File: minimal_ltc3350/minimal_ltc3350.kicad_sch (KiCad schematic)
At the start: 43 parts, among them Q1 20.0 V, Q2 20.0 V, Q3 20 V, Q4 20 V, U1 LTC3350EUHF-PBF

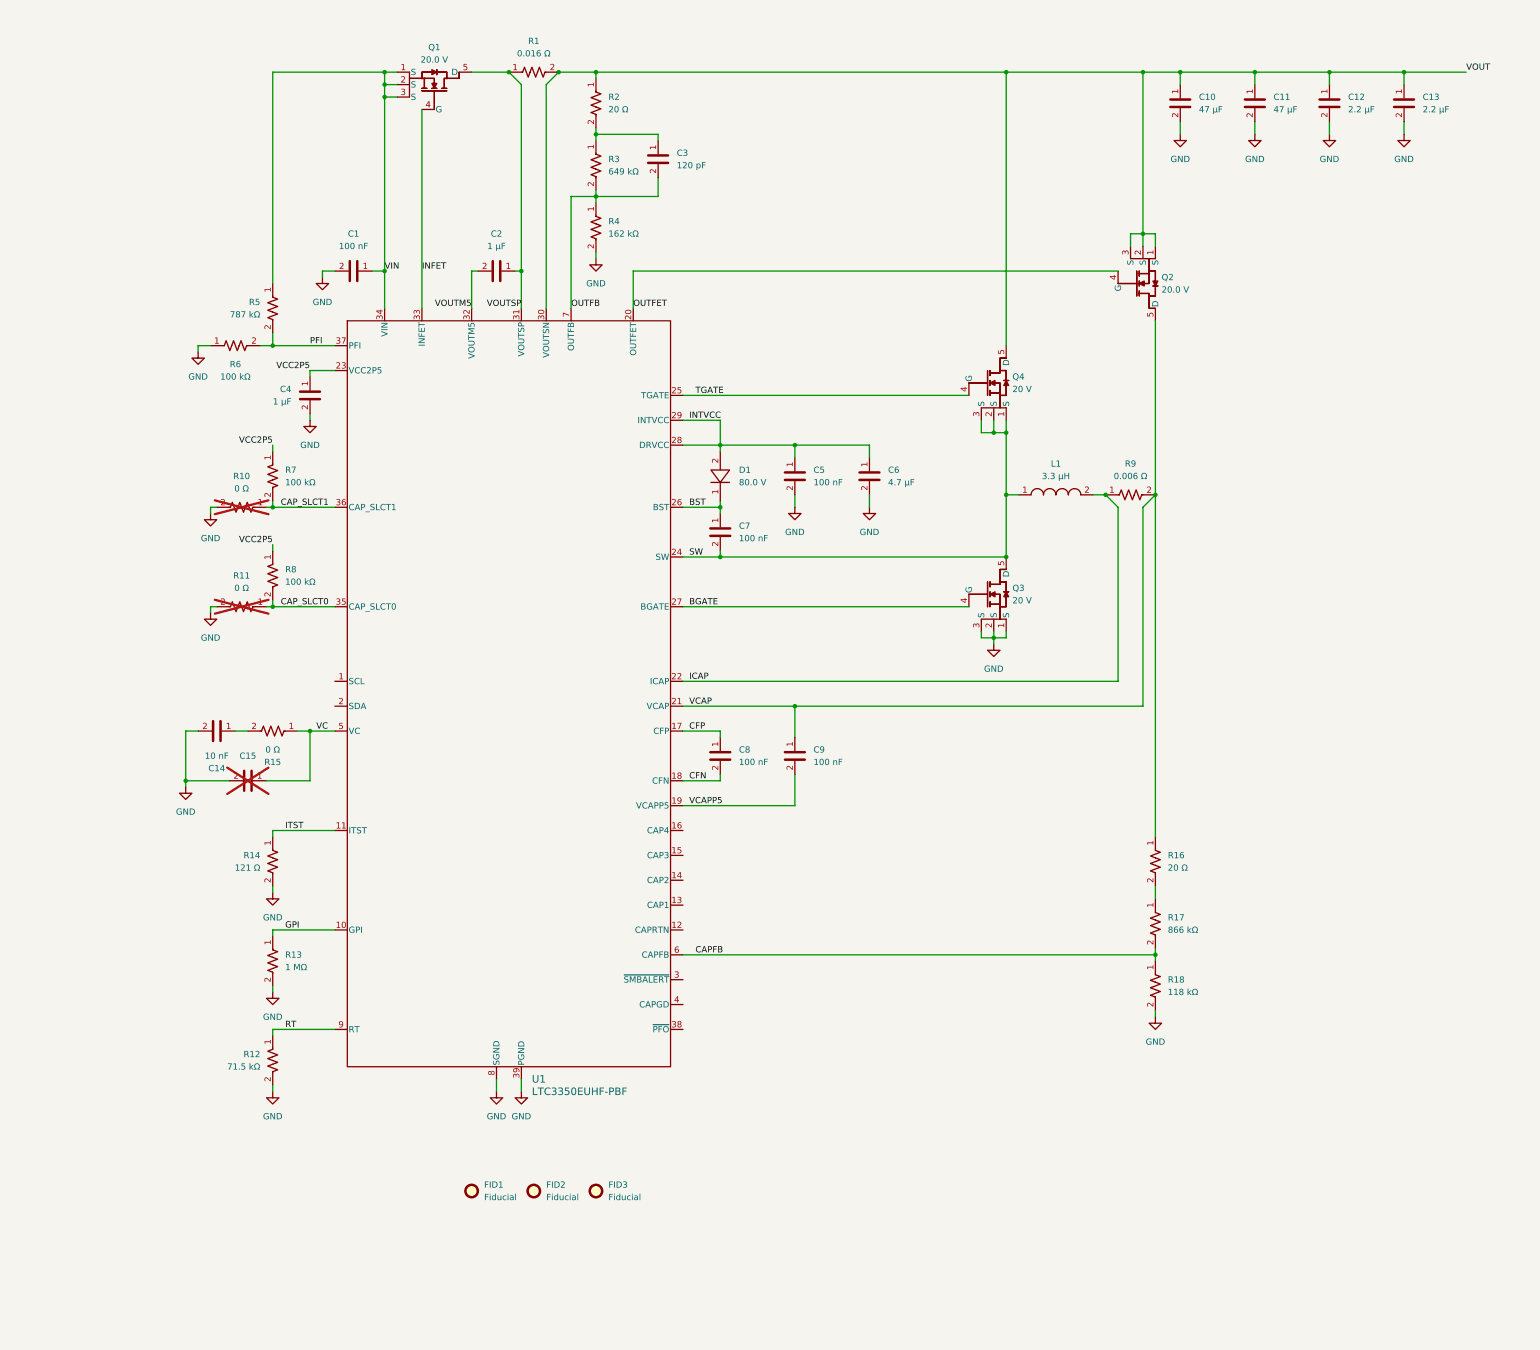
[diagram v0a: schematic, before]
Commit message: Add C19 capacitor and update component positions in KiCad project
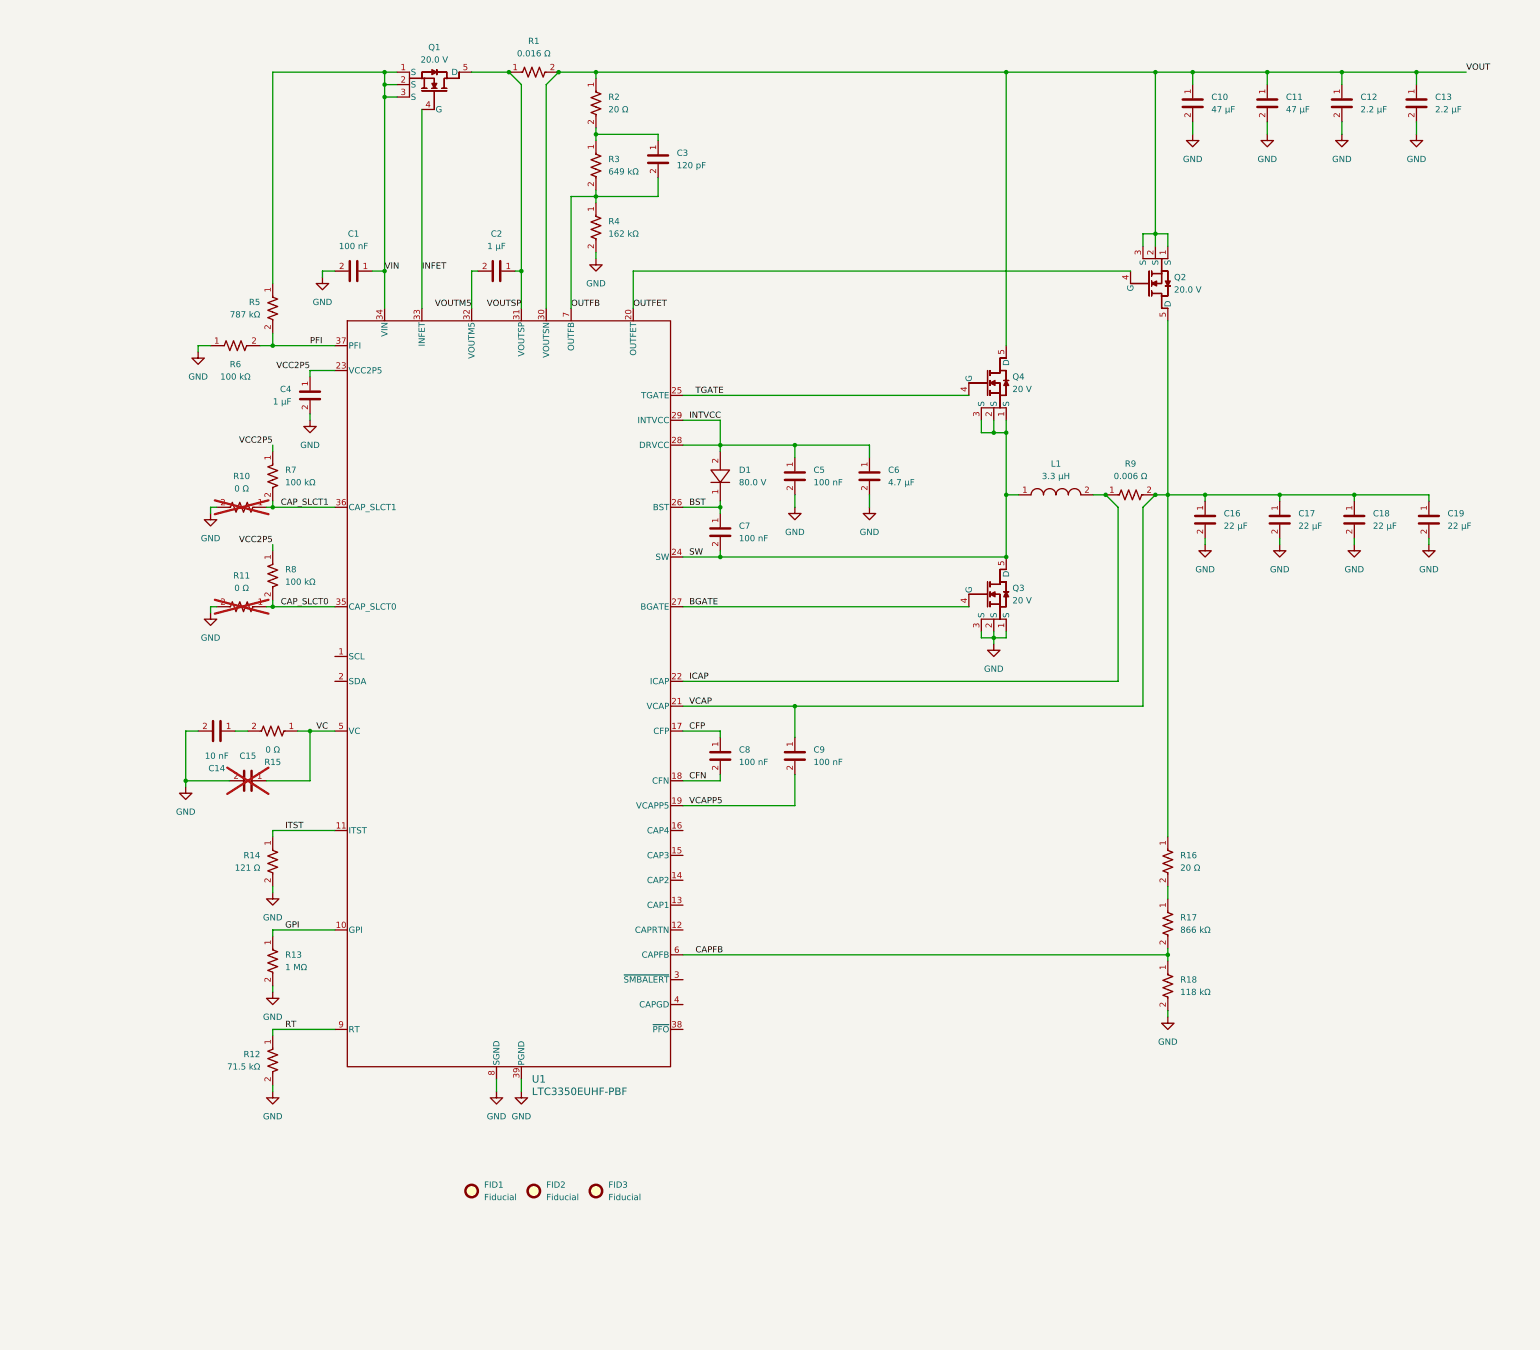
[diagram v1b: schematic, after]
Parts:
- added C16, C17, C18, C19: 22 µF, capacitor_footprints:C_0805_2012Metric, symbol CAPACITORS_C2012X5R1C_DATA_BASE:C_C2012X5R1C226M125AC
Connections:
- net GND: now also C16.2, C17.2, C18.2, C19.2
- net VCAP: now also C16.1, C17.1, C18.1, C19.1
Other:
- moved on the sheet: C10, C11, C12, C13, Q2, R16, R17, R18

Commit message: Update KiCAD project files and symbols generator
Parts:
- added R19, R20, R21, R22, R23: 2.7 Ω, resistor_footprints:R_0805_2012Metric, symbol RESISTORS_ERJ-6DQF_DATA_BASE:R_ERJ-6DQF2R7V
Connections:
- net GND: now also R23.2
- net VCAP: now also R19.2
- net CAPRTN: now reaches U1.12 (CAPRTN)
- net CAPRTN: now also R23.1
- net CAP1: now reaches U1.13 (CAP1)
- net CAP1: now also R22.1
- net CAP2: now reaches U1.14 (CAP2)
- net CAP2: now also R21.1
- net CAP3: now reaches U1.15 (CAP3)
- net CAP3: now also R20.1
- net CAP4: now reaches U1.16 (CAP4)
- net CAP4: now also R19.1
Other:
- moved on the sheet: C1, C10, C11, C12, C13, C14, C15, C16, C17, C18, C19, C2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

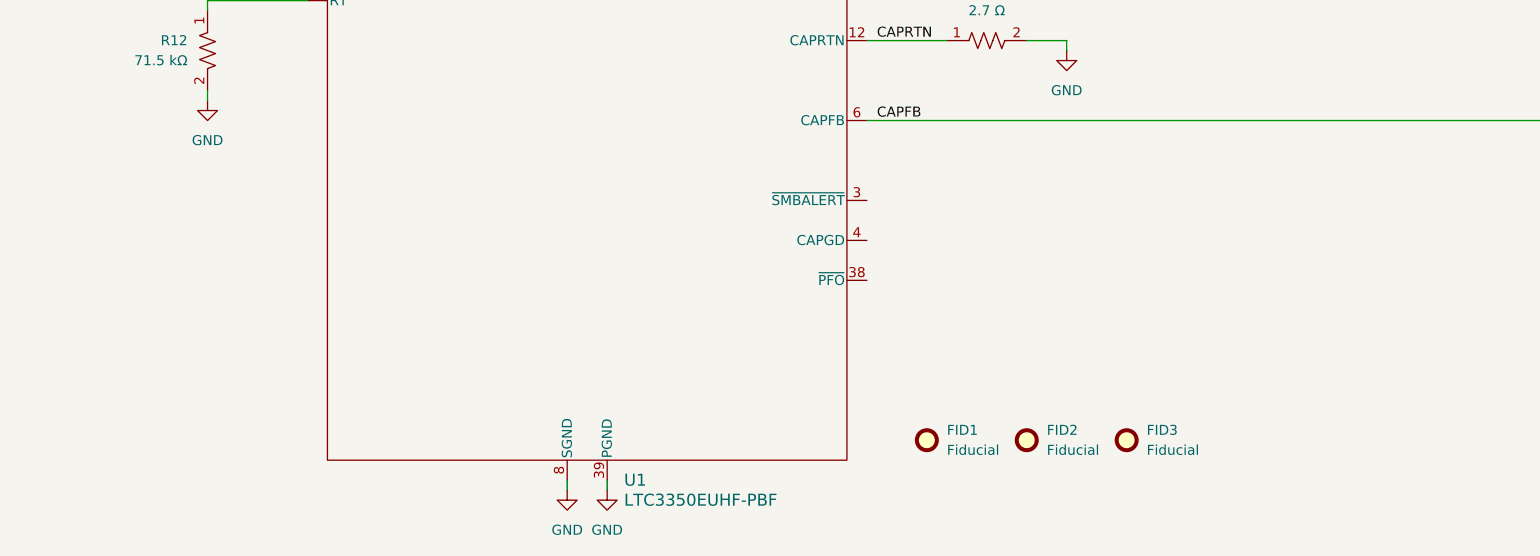
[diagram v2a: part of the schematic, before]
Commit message: Update KiCad project: Add LED components and adjust resistor positions
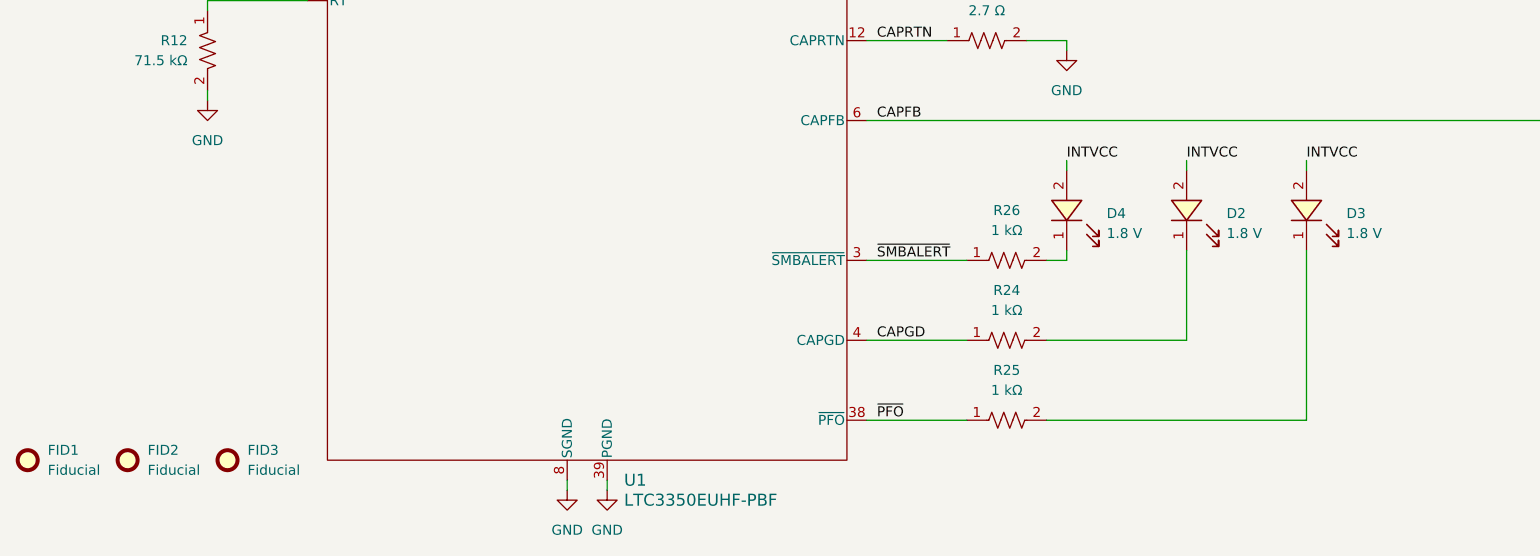
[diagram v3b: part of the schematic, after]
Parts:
- added D2, D3, D4: 1.8 V, diode_footprints:LED_RED_0402_1005Metric, symbol DIODES_APHHS1005LSECK-J3-PF_DATA_BASE:D_APHHS1005LSECK-J3-PF
- added R24, R25, R26: 1 kΩ, resistor_footprints:R_0402_1005Metric, symbol RESISTORS_ERJ-2RKF_DATA_BASE:R_ERJ-2RKF1001X
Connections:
- net INTVCC: now also D2.2, D3.2, D4.2
- net ~{SMBALERT}: now reaches U1.3 (~{SMBALERT})
- net ~{SMBALERT}: now also R26.1
- net ~{PFO}: now reaches U1.38 (~{PFO})
- net ~{PFO}: now also R25.1
- net CAPGD: now reaches U1.4 (CAPGD)
- net CAPGD: now also R24.1
- new net: D2.1, R24.2
- new net: D4.1, R26.2
- new net: D3.1, R25.2
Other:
- moved on the sheet: FID1, FID2, FID3

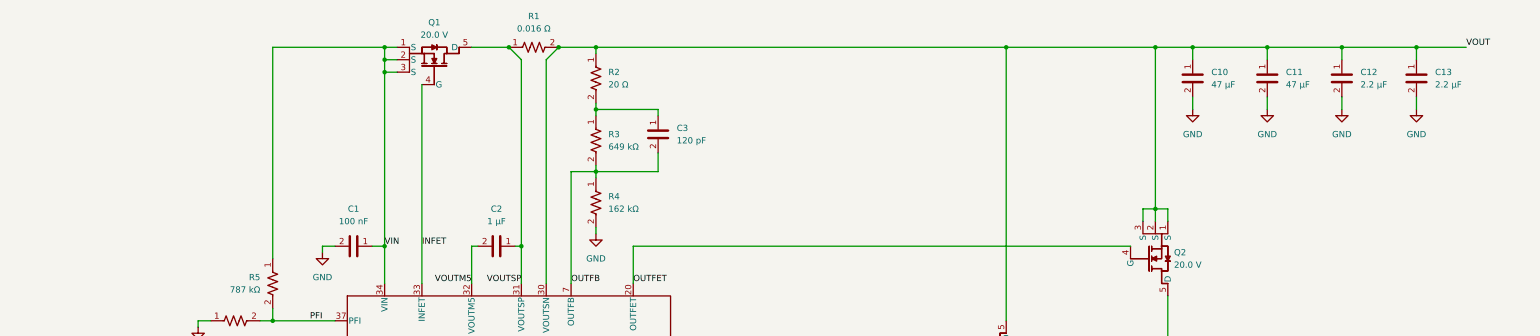
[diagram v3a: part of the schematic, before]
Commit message: Update KiCad project: Update PCB layout and schematic
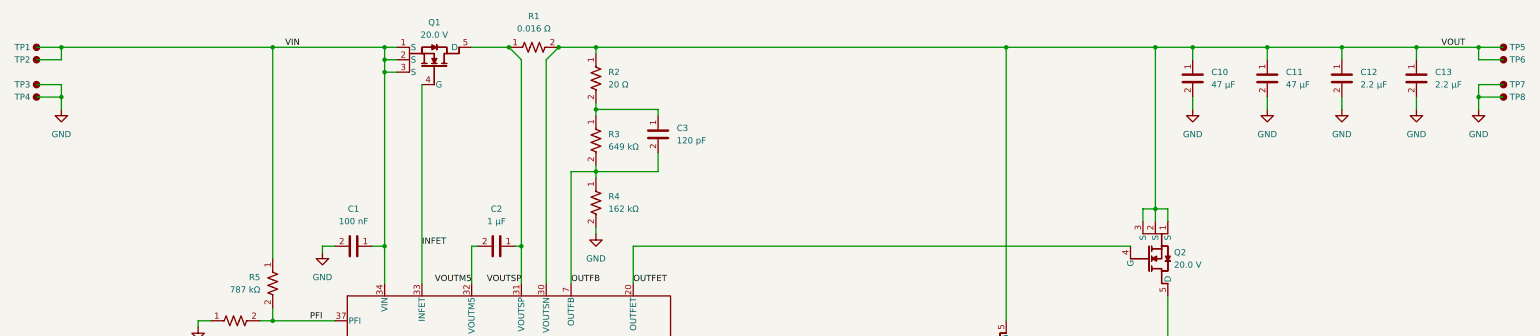
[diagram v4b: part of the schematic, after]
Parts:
- added TP1, TP2, TP3, TP4, TP5, TP6, TP7, TP8: TestPoint, test_point_footprints:TestPoint_THTPad_Castelated, symbol UNITED_TEST_POINTS:TestPoint_Castelated_v2
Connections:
- net GND: now also TP3.1, TP4.1, TP7.1, TP8.1
- net VIN: now also TP1.1, TP2.1
- net VOUT: now also TP5.1, TP6.1

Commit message: Update KiCAD files and symbol table
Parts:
- removed R14: 121 Ω, resistor_footprints:R_0402_1005Metric, symbol RESISTORS_ERJ-2RKF_DATA_BASE:R_ERJ-2RKF1210X
- added Q5: 20.0 V, transistor_footprints:SOT23, symbol TRANSISTORS_SI2374DS-T1-BE3_DATA_BASE:Q_SI2374DS-T1-BE3
- added R27: 10 MΩ, resistor_footprints:R_0402_1005Metric, symbol RESISTORS_RC0402FR-07_DATA_BASE:R_RC0402FR-0710ML
- added R28, R29: 100 Ω, resistor_footprints:R_2512_6332Metric, symbol RESISTORS_SR2512FK-7W_DATA_BASE:R_SR2512FK-7W100RL
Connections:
- net GND: now also Q5.3 (D), R27.2
- net ITST: now also Q5.1 (G), R27.1
- net VCAP: now also R28.1, R29.1
- new net: Q5.2 (S), R28.2, R29.2
